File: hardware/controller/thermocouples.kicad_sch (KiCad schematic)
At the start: 9 parts, among them J1 Conn_01x02_Pin, J2 Conn_01x02_Pin, J3 Conn_01x02_Pin, U2 MAX31855KASA, U3 MAX31855KASA, U4 MAX31855KASA

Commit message: Add filtering caps to thermocouples
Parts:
- added C14, C15, C16: 10nF, Capacitor_SMD:C_0805_2012Metric, symbol Device:C
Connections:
- net at J3.1 (Pin_1), U4.2 (T-): now also C15.2
- net at J3.2 (Pin_2), U4.3 (T+): now also C15.1
- net at J2.1 (Pin_1), U3.2 (T-): now also C16.2
- net at J2.2 (Pin_2), U3.3 (T+): now also C16.1
- net at J1.1 (Pin_1), U2.2 (T-): now also C14.2
- net at J1.2 (Pin_2), U2.3 (T+): now also C14.1
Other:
- moved on the sheet: C4, J1, J2, J3, U3

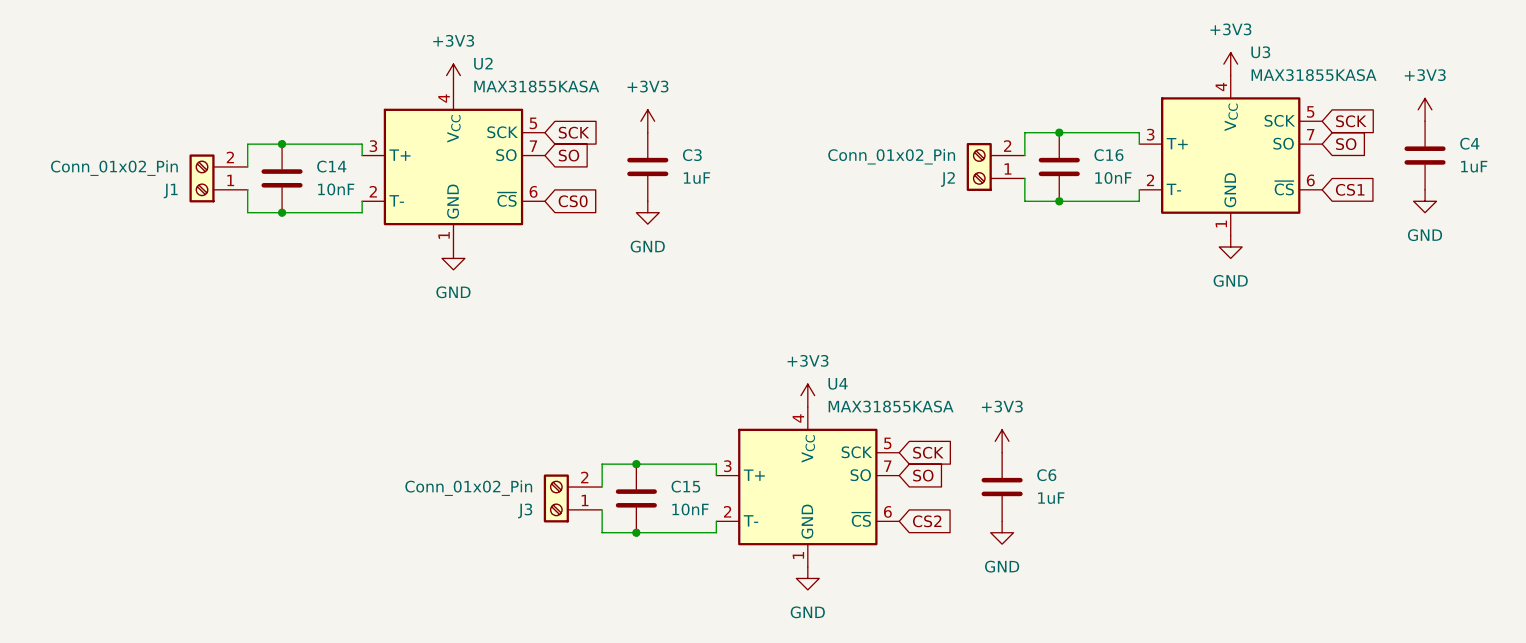
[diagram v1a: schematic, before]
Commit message: Add linear regulator for MAX chips
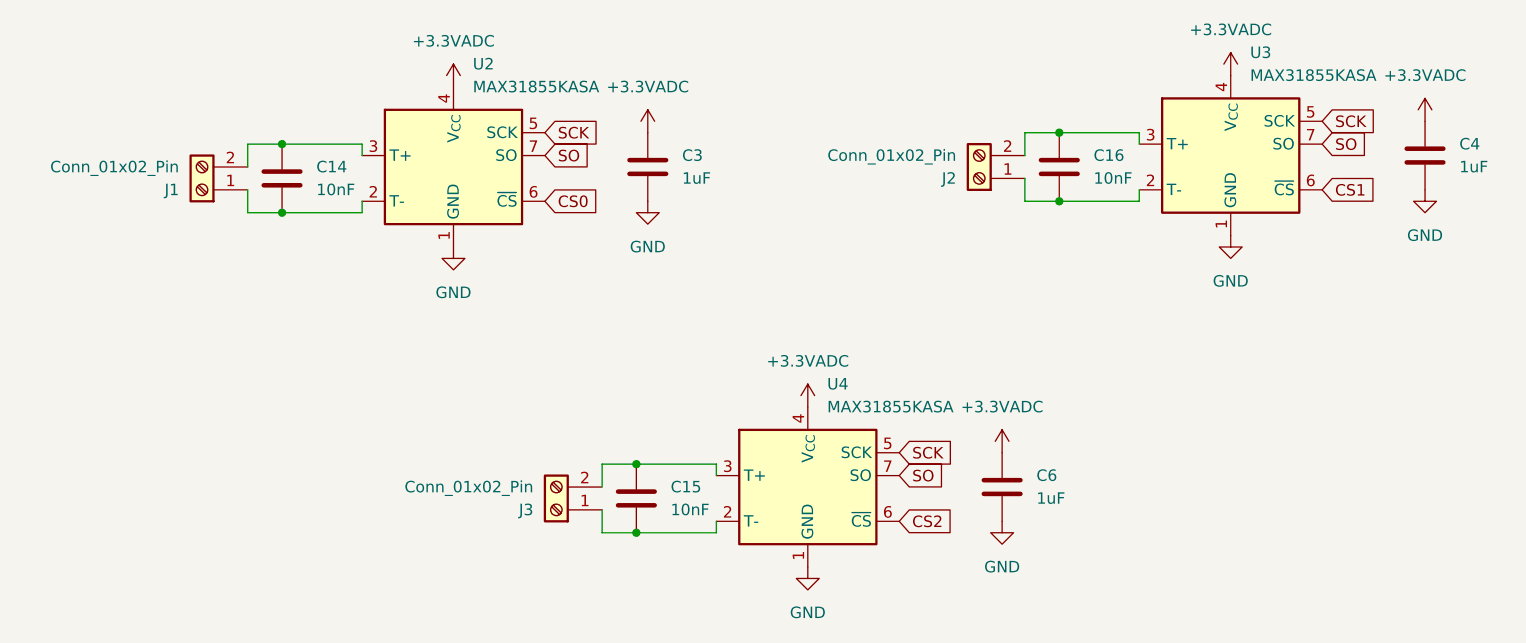
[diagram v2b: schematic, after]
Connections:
- net +3V3 renamed +3.3VADC

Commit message: Increase capacitance of MAX caps
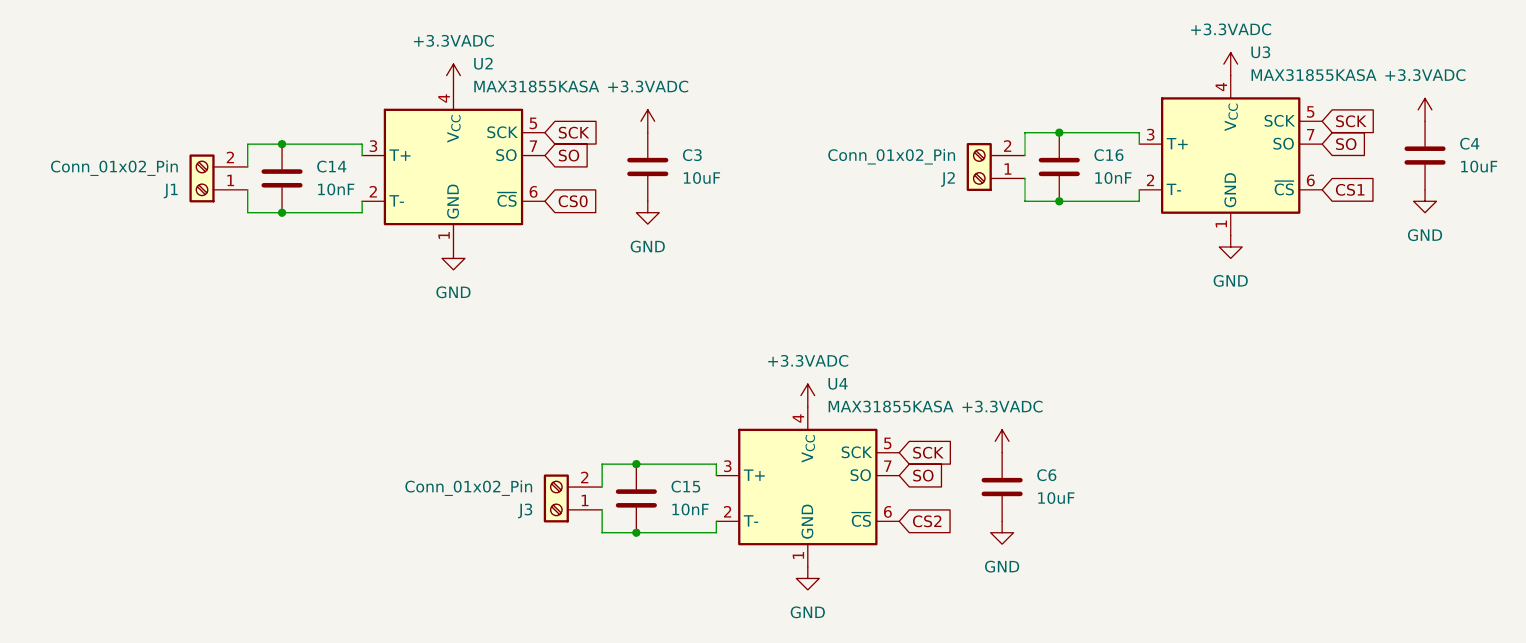
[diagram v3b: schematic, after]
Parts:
- C3, C4, C6: value 1uF -> 10uF; LCSC C28323 -> C15850
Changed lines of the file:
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@@
 			)
 		)
-		(property "Value" "1uF"
+		(property "Value" "10uF"
 			(at 168.91 106.6799 0)
 			(effects
@@
 			)
 		)
-		(property "LCSC" "C28323"
+		(property "LCSC" "C15850"
 			(at 165.1 105.41 0)
 			(effects
@@
 			)
 		)
-		(property "Value" "1uF"
+		(property "Value" "10uF"
 			(at 129.54 71.1199 0)
 			(effects
@@
 			)
 		)
-		(property "LCSC" "C28323"
+		(property "LCSC" "C15850"
 			(at 125.73 69.85 0)
 			(effects
@@
 			)
 		)
-		(property "Value" "1uF"
+		(property "Value" "10uF"
 			(at 215.9 69.8499 0)
 			(effects
@@
 			)
 		)
-		(property "LCSC" "C28323"
+		(property "LCSC" "C15850"
 			(at 212.09 68.58 0)
 			(effects
